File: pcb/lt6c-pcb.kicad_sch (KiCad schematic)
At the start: 19 parts, among them SW1 SW_Push, SW2 SW_Push, SW3 SW_Push, SW4 SW_Push, SW5 SW_Push, SW6 SW_Push, U1 XIAO-RP2040, U2 TPS76318, U3 PMW3360DM-T2QU

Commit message: Update README.md & .gitattributes
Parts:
- H1, H2, H3, H4: value MountingHole_M2 -> MountingHole_Pad
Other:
- moved on the sheet: H1, H2, H3, H4
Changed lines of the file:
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@@
 	)
 	(no_connect
-		(at 155.575 21.59)
+		(at 151.13 19.05)
 	)
 	(no_connect
-		(at 155.575 29.21)
+		(at 151.13 26.67)
 	)
 	(no_connect
-		(at 155.575 44.45)
+		(at 151.13 41.91)
 	)
 	(no_connect
@@
 	)
 	(no_connect
-		(at 155.575 36.83)
+		(at 151.13 34.29)
 	)
 	(wire
@@
 	)
 	(rectangle
-		(start 151.13 46.99)
+		(start 147.955 46.99)
 		(end 177.8 50.165)
 		(stroke
@@
 	)
 	(rectangle
-		(start 100.33 51.435)
-		(end 177.8 106.045)
+		(start 59.69 46.99)
+		(end 81.28 50.165)
 		(stroke
 			(width 0)
@@
 	)
 	(rectangle
-		(start 59.944 46.99)
-		(end 81.28 50.165)
+		(start 77.47 102.87)
+		(end 99.06 106.045)
 		(stroke
 			(width 0)
@@
 	)
 	(rectangle
-		(start 82.55 13.97)
-		(end 149.86 50.165)
+		(start 100.33 51.435)
+		(end 177.8 106.045)
 		(stroke
 			(width 0)
@@
 	)
 	(rectangle
-		(start 151.13 13.97)
-		(end 177.8 50.165)
+		(start 156.21 102.87)
+		(end 177.8 106.045)
 		(stroke
 			(width 0)
@@
 	)
 	(rectangle
-		(start 161.925 102.87)
-		(end 177.8 106.045)
+		(start 82.55 13.97)
+		(end 146.685 50.165)
 		(stroke
 			(width 0)
@@
 	)
 	(rectangle
-		(start 134.62 46.99)
-		(end 149.86 50.165)
+		(start 147.955 13.97)
+		(end 177.8 50.165)
 		(stroke
 			(width 0)
@@
 	)
 	(rectangle
-		(start 80.01 102.87)
-		(end 99.06 106.045)
+		(start 125.095 46.99)
+		(end 146.685 50.165)
 		(stroke
 			(width 0)
@@
 	(text "PMW3360 LDO"
 		(exclude_from_sim no)
-		(at 142.24 48.895 0)
+		(at 135.89 48.895 0)
 		(effects
 			(font
@@
 	(text "Mounting Holes"
 		(exclude_from_sim no)
-		(at 164.465 48.895 0)
+		(at 162.56 48.895 0)
 		(effects
 			(font
@@
 	(text "PMW3360 Sensor"
 		(exclude_from_sim no)
-		(at 89.535 104.775 0)
+		(at 88.265 104.775 0)
 		(effects
 			(font
@@
 	(text "Mouse Buttons"
 		(exclude_from_sim no)
-		(at 170.18 104.775 0)
+		(at 167.005 104.775 0)
 		(effects
 			(font
@@
 	(symbol
 		(lib_id "Mechanical:MountingHole_Pad")
-		(at 155.575 19.05 0)
+		(at 153.67 19.05 270)
 		(unit 1)
 		(exclude_from_sim yes)
@@
 		(fields_autoplaced yes)
 		(property "Reference" "H1"
-			(at 158.75 16.5099 0)
+			(at 158.115 17.7799 90)
 			(effects
 				(font
@@
 			)
 		)
-		(property "Value" "MountingHole_M2"
-			(at 158.75 19.0499 0)
+		(property "Value" "MountingHole_Pad"
+			(at 158.115 20.3199 90)
 			(effects
 				(font
@@
 		)
 		(property "Footprint" "MountingHole:MountingHole_2.2mm_M2_ISO14580_Pad"
-			(at 155.575 19.05 0)
+			(at 153.67 19.05 0)
 			(effects
 				(font
@@
 		)
 		(property "Datasheet" "~"
-			(at 155.575 19.05 0)
+			(at 153.67 19.05 0)
 			(effects
 				(font
@@
 		)
 		(property "Description" "Mounting Hole with connection"
-			(at 155.575 19.05 0)
+			(at 153.67 19.05 0)
 			(effects
 				(font
@@
 		)
 		(property "JLC" ""
-			(at 155.575 19.05 0)
+			(at 153.67 19.05 0)
 			(effects
 				(font
@@
 		)
 		(property "JLCPosOffset" ""
-			(at 155.575 19.05 0)
+			(at 153.67 19.05 0)
 			(effects
 				(font
@@
 		)
 		(property "JLCRotOffset" ""
-			(at 155.575 19.05 0)
+			(at 153.67 19.05 0)
 			(effects
 				(font
@@
 		)
 		(property "LCSC" ""
-			(at 155.575 19.05 0)
+			(at 153.67 19.05 0)
 			(effects
 				(font
@@
 	(symbol
 		(lib_id "Mechanical:MountingHole_Pad")
-		(at 155.575 26.67 0)
+		(at 153.67 26.67 270)
 		(unit 1)
 		(exclude_from_sim yes)
@@
 		(fields_autoplaced yes)
 		(property "Reference" "H2"
-			(at 158.75 24.1299 0)
+			(at 158.115 25.3999 90)
 			(effects
 				(font
@@
 			)
 		)
-		(property "Value" "MountingHole_M2"
-			(at 158.75 26.6699 0)
+		(property "Value" "MountingHole_Pad"
+			(at 158.115 27.9399 90)
 			(effects
 				(font
@@
 		)
 		(property "Footprint" "MountingHole:MountingHole_2.2mm_M2_ISO14580_Pad"
-			(at 155.575 26.67 0)
+			(at 153.67 26.67 0)
 			(effects
 				(font
@@
 		)
 		(property "Datasheet" "~"
-			(at 155.575 26.67 0)
+			(at 153.67 26.67 0)
 			(effects
 				(font
@@
 		)
 		(property "Description" "Mounting Hole with connection"
-			(at 155.575 26.67 0)
+			(at 153.67 26.67 0)
 			(effects
 				(font
@@
 		)
 		(property "JLC" ""
-			(at 155.575 26.67 0)
+			(at 153.67 26.67 0)
 			(effects
 				(font
@@
 		)
 		(property "JLCPosOffset" ""
-			(at 155.575 26.67 0)
+			(at 153.67 26.67 0)
 			(effects
 				(font
@@
 		)
 		(property "JLCRotOffset" ""
-			(at 155.575 26.67 0)
+			(at 153.67 26.67 0)
 			(effects
 				(font
@@
 		)
 		(property "LCSC" ""
-			(at 155.575 26.67 0)
+			(at 153.67 26.67 0)
 			(effects
 				(font
@@
 	(symbol
 		(lib_id "Mechanical:MountingHole_Pad")
-		(at 155.575 41.91 0)
+		(at 153.67 41.91 270)
 		(unit 1)
 		(exclude_from_sim yes)
@@
 		(fields_autoplaced yes)
 		(property "Reference" "H4"
-			(at 158.75 39.3699 0)
+			(at 158.115 40.6399 90)
 			(effects
 				(font
@@
 			)
 		)
-		(property "Value" "MountingHole_M2"
-			(at 158.75 41.9099 0)
+		(property "Value" "MountingHole_Pad"
+			(at 158.115 43.1799 90)
 			(effects
 				(font
@@
 		)
 		(property "Footprint" "MountingHole:MountingHole_2.2mm_M2_ISO14580_Pad"
-			(at 155.575 41.91 0)
+			(at 153.67 41.91 0)
 			(effects
 				(font
@@
 		)
 		(property "Datasheet" "~"
-			(at 155.575 41.91 0)
+			(at 153.67 41.91 0)
 			(effects
 				(font
@@
 		)
 		(property "Description" "Mounting Hole with connection"
-			(at 155.575 41.91 0)
+			(at 153.67 41.91 0)
 			(effects
 				(font
@@
 		)
 		(property "JLC" ""
-			(at 155.575 41.91 0)
+			(at 153.67 41.91 0)
 			(effects
 				(font
@@
 		)
 		(property "JLCPosOffset" ""
-			(at 155.575 41.91 0)
+			(at 153.67 41.91 0)
 			(effects
 				(font
@@
 		)
 		(property "JLCRotOffset" ""
-			(at 155.575 41.91 0)
+			(at 153.67 41.91 0)
 			(effects
 				(font
@@
 		)
 		(property "LCSC" ""
-			(at 155.575 41.91 0)
+			(at 153.67 41.91 0)
 			(effects
 				(font
@@
 	(symbol
 		(lib_id "Mechanical:MountingHole_Pad")
-		(at 155.575 34.29 0)
+		(at 153.67 34.29 270)
 		(unit 1)
 		(exclude_from_sim yes)
@@
 		(fields_autoplaced yes)
 		(property "Reference" "H3"
-			(at 158.75 31.7499 0)
+			(at 158.115 33.0199 90)
 			(effects
 				(font
@@
 			)
 		)
-		(property "Value" "MountingHole_M2"
-			(at 158.75 34.2899 0)
+		(property "Value" "MountingHole_Pad"
+			(at 158.115 35.5599 90)
 			(effects
 				(font
@@
 		)
 		(property "Footprint" "MountingHole:MountingHole_2.2mm_M2_ISO14580_Pad"
-			(at 155.575 34.29 0)
+			(at 153.67 34.29 0)
 			(effects
 				(font
@@
 		)
 		(property "Datasheet" "~"
-			(at 155.575 34.29 0)
+			(at 153.67 34.29 0)
 			(effects
 				(font
@@
 		)
 		(property "Description" "Mounting Hole with connection"
-			(at 155.575 34.29 0)
+			(at 153.67 34.29 0)
 			(effects
 				(font
@@
 		)
 		(property "JLC" ""
-			(at 155.575 34.29 0)
+			(at 153.67 34.29 0)
 			(effects
 				(font
@@
 		)
 		(property "JLCPosOffset" ""
-			(at 155.575 34.29 0)
+			(at 153.67 34.29 0)
 			(effects
 				(font
@@
 		)
 		(property "JLCRotOffset" ""
-			(at 155.575 34.29 0)
+			(at 153.67 34.29 0)
 			(effects
 				(font
@@
 		)
 		(property "LCSC" ""
-			(at 155.575 34.29 0)
+			(at 153.67 34.29 0)
 			(effects
 				(font

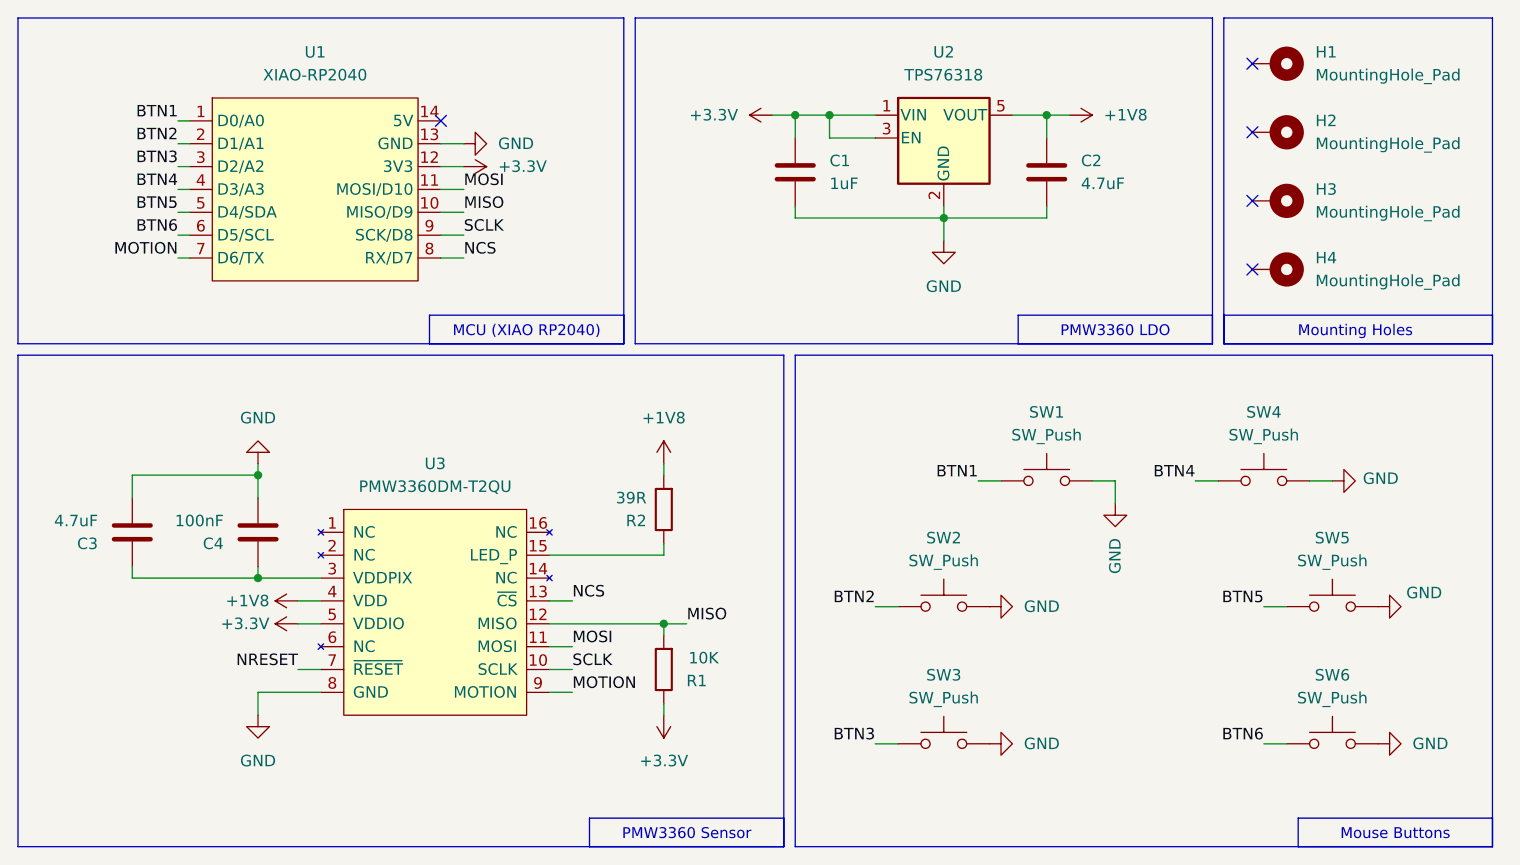
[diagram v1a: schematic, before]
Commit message: Fix ERC/DRC + update LKBD libraries
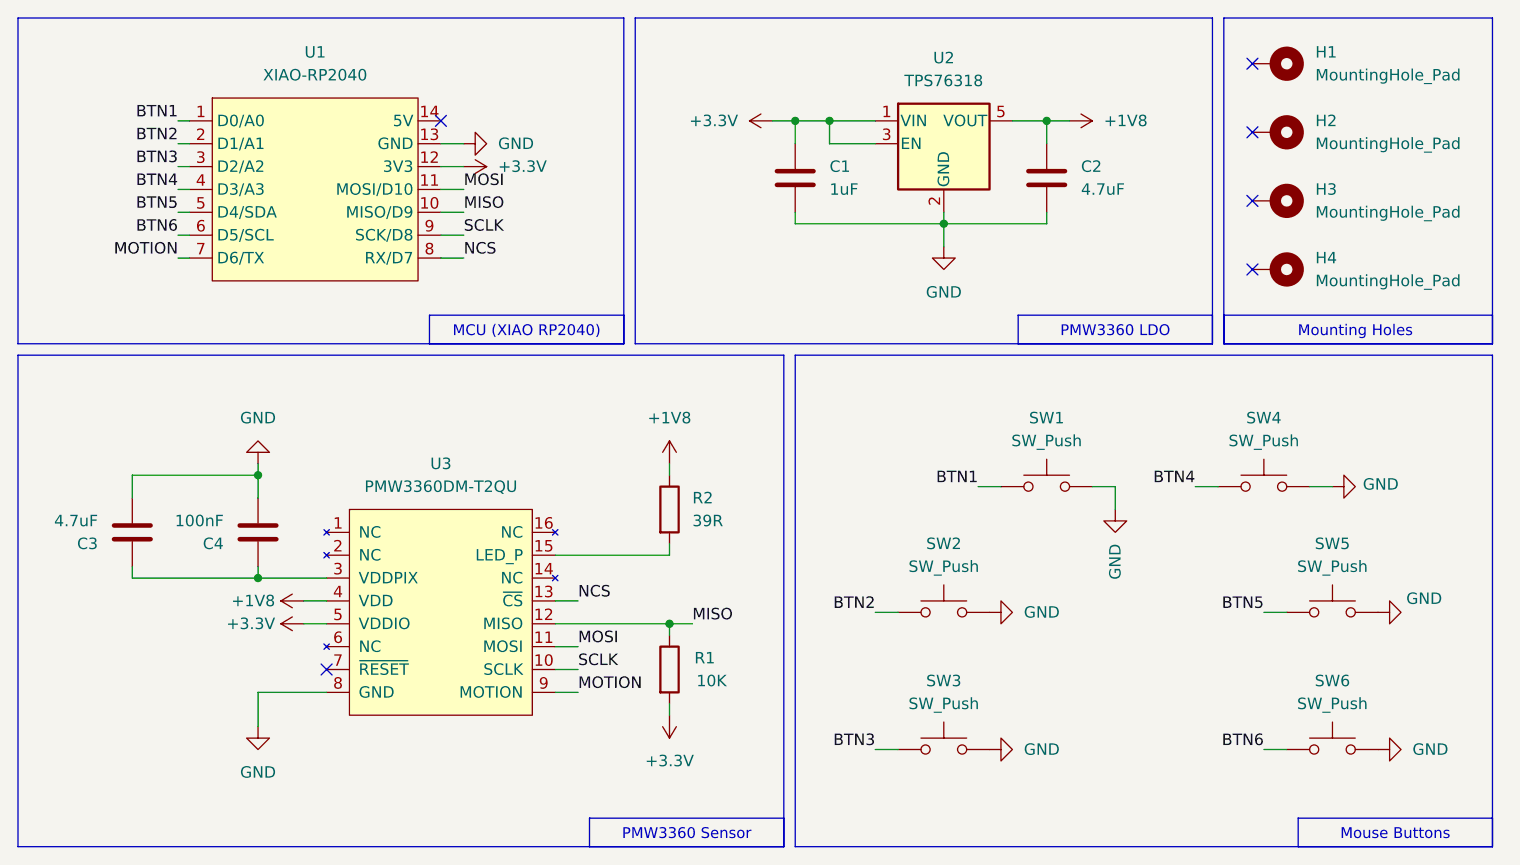
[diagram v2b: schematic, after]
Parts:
- R1, R2: symbol PCM_SL_Resistors:Resistor -> Device:R
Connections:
- net NRESET: no longer names the net of U3.7 (~{RESET})
- no-connect marks 5 -> 6
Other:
- moved on the sheet: C1, C2, R1, R2, SW1, SW2, SW3, SW4, SW5, SW6, U2, U3
